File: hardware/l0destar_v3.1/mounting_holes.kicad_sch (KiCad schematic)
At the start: 4 parts

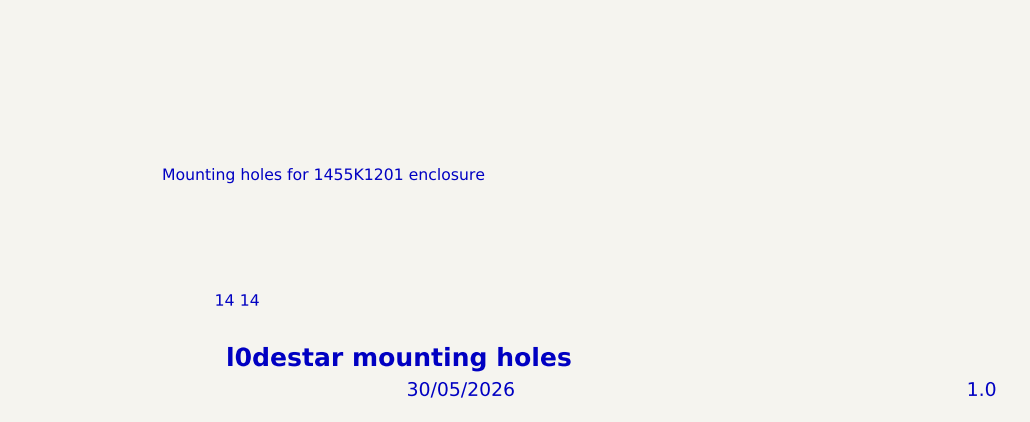
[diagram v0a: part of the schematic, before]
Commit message: update sheet annotations
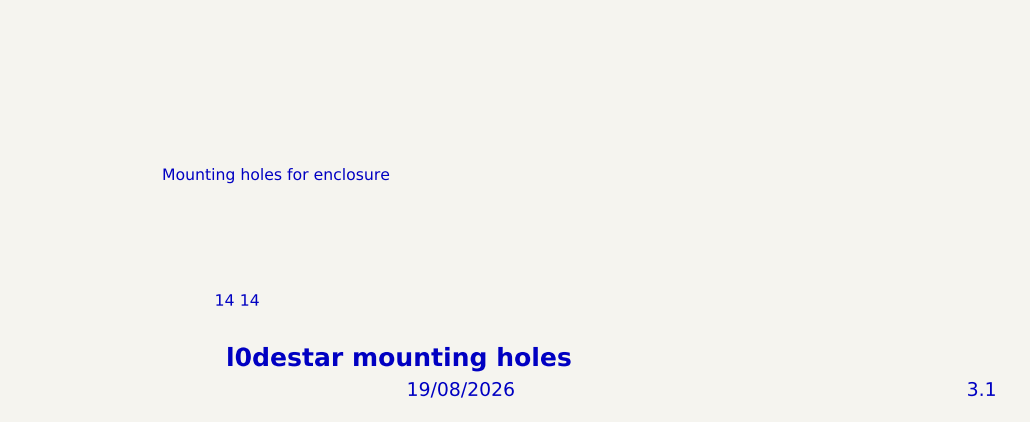
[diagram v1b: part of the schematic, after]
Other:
- note added: "19/08/2026"
- note added: "3.1"
- note added: "Mounting holes for enclosure"
- note removed: "1.0"
- note removed: "30/05/2026"
- note removed: "Mounting holes for 1455K1201 enclosure"
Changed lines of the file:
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@@
 		)
 	)
-	(text "Mounting holes for 1455K1201 enclosure"
+	(text "Mounting holes for enclosure"
 		(exclude_from_sim no)
 		(at 179.07 169.418 0)
@@
 		)
 	)
-	(text "1.0"
+	(text "3.1"
 		(exclude_from_sim no)
 		(at 268.478 193.294 0)
@@
 		)
 	)
-	(text "30/05/2026"
+	(text "19/08/2026"
 		(exclude_from_sim no)
 		(at 206.248 193.294 0)
